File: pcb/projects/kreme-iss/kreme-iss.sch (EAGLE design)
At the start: 89 parts, among them IC1 ADG609RU, IC3 ADG609RU, P1 53048-0810, P2 53048-0810, U1 MCP73831/OT, U10 MAX31855KASA+T21-0041B_8-M, U11 MAX31855KASA+T21-0041B_8-M, U2 LP2985IM5-1.8/NOPB, U3 COM-13909, U4 ADXL377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

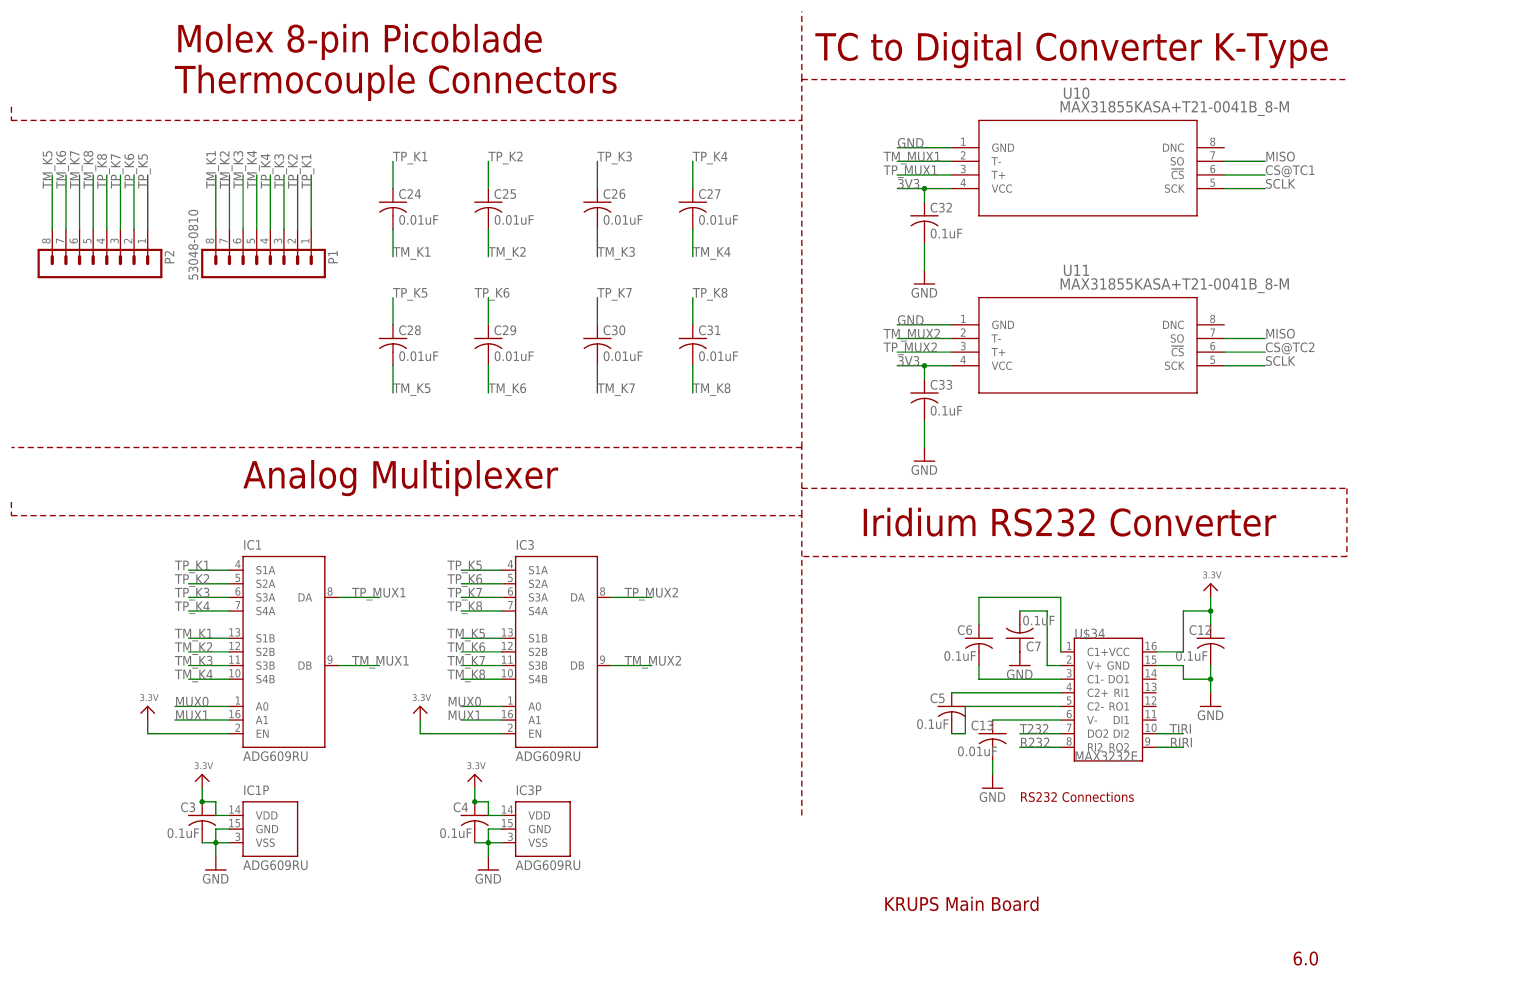
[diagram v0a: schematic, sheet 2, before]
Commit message: v1.1 update
Updates to the flight computer:
* update to max31856 tc to digital to support k/j type tc as well as 7
other types
* add pins for iridium sbd message ready and iridium actively
transmitting
* add capacity sense header
* add through hole connection for battery
* remove rs232 level converter - all pins are 5v tolerant on teensy 3.5
and the iridium operates from 3.5-5.5v DC so no need for it
* add imu orientation silk screen as well as arduino pin map silk on
back
* more meaningful LED names
* added end-to-end activation and battery protection schematic

Other updates
* documentation tex file is now local
* add battery protection schematic, board and gerbers as well as renders
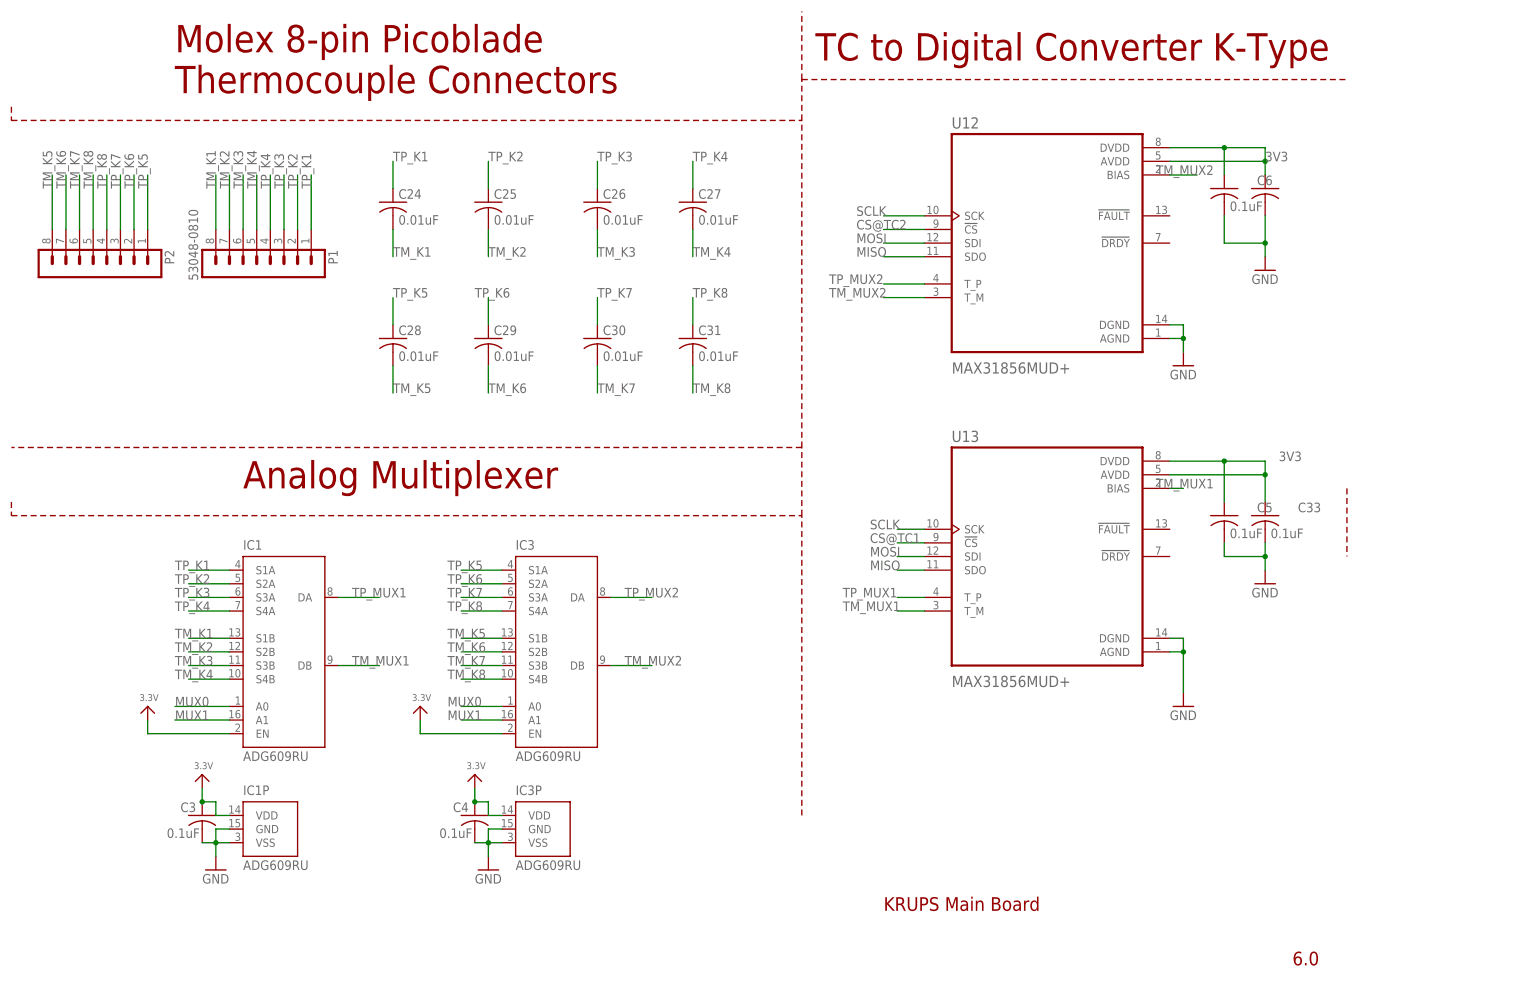
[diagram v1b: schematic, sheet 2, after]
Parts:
- removed C12, C7: 0.1uF, adafruit:C-USC0603
- removed C13: 0.01uF, adafruit:C-USC0603
- removed LED6, LED7, LED8: (no value), adafruit:LEDCHIP-LED0603
- removed R12, R16, R17: 470, rcl:R-US_R0603
- removed U$34: MAX3232E, TI_radio:MAX3232E
- removed U10, U11: MAX31855KASA+T21-0041B_8-M, max31855:MAX31855KASA+T21-0041B_8-M
- added CAPSENSE: 53048-0810, con-molex-picoblade:53048-0810
- added U12, U13: MAX31856MUD+, MAX31856:MAX31856MUD+
- added VBAT_PTH: (no value), pinhead:PINHD-1X2
- renumbered POWER_SW to ACTIVATION_SW
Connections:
- removed net LED6: R12.1, U$1.8
- removed net LED7: R16.1, U$1.24
- removed net LED8: R17.1, U$1.25
- removed net N$10: C6.2, U$34.C1-
- removed net N$11: C5.1, U$34.C2+
- removed net N$14: C13.1, U$34.V-
- removed net N$17: C7.2, U$34.V+
- removed net N$29: LED6.A, R12.2
- removed net N$30: LED7.A, R16.2
- removed net N$31: LED8.A, R17.2
- removed net N$5: C5.2, U$34.C2-
- removed net N$8: C6.1, U$34.C1+
- removed net R232: U$34.RI2, X3.2
- removed net T232: U$34.DO2, X3.1
- new net CAPSENSE0: CAPSENSE.4, U$1.0/RX
- new net CAPSENSE1: CAPSENSE.2, U$1.1/TX
- new net CAPSENSE2: CAPSENSE.6, U$1.15/A1
- new net CAPSENSE3: CAPSENSE.8, U$1.30
- new net IRIDIUM_STATUS: U$1.A22/DAC1, X3.5
- new net IRIDIUM_TX_ACT: U$1.A21/DAC0, X3.6
- net 3V3: now also C5.1, C6.1, U12.AVDD, U12.DVDD, U13.AVDD, U13.DVDD; no longer C12.1, U$34.VCC, U10.VCC, U11.VCC
- net CS@TC1: now also U13.!CS; no longer U10.!CS
- net CS@TC2: now also U12.!CS; no longer U11.!CS
- net GND: now also C5.2, C6.2, CAPSENSE.1, CAPSENSE.3, CAPSENSE.5, CAPSENSE.7, U12.AGND, U12.DGND, U13.AGND, U13.DGND, VBAT_PTH.1, X3.2; no longer C12.2, C13.2, C7.1, LED6.C, LED7.C, LED8.C, U$34.GND, U10.GND, U11.GND, X3.5, X3.6
- net MISO: now also U12.SDO, U13.SDO; no longer U10.SO, U11.SO
- net MOSI: now also U12.SDI, U13.SDI
- net RIRI: now also X3.4; no longer U$34.RO2
- net SCLK: now also U12.SCK, U13.SCK; no longer U10.SCK, U11.SCK
- net TIRI: now also X3.3; no longer U$34.DI2
- net TM_MUX1: now also U13.BIAS, U13.T_M; no longer U10.T-
- net TM_MUX2: now also U12.BIAS, U12.T_M; no longer U11.T-
- net TP_MUX1: now also U13.T_P; no longer U10.T+
- net TP_MUX2: now also U12.T_P; no longer U11.T+
- net V+_IRIDIUM: now also X3.1; no longer X3.3, X3.4
- net VBAT: now also VBAT_PTH.2
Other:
- note added: "Capacitive Sense Header"
- note removed: "Iridium RS232 Converter"
- note removed: "RS232 Connections"
- moved on the sheet: C33, C5, C6, X3
